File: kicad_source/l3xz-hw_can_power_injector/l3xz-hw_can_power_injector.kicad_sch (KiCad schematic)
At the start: 30 parts, among them CN1 Conn_01x02, CN2 Conn_01x04, CN3 Conn_01x04, CN4 Conn_01x02, CN5 Conn_01x04, CN6 Conn_01x04, U1 RAA211650

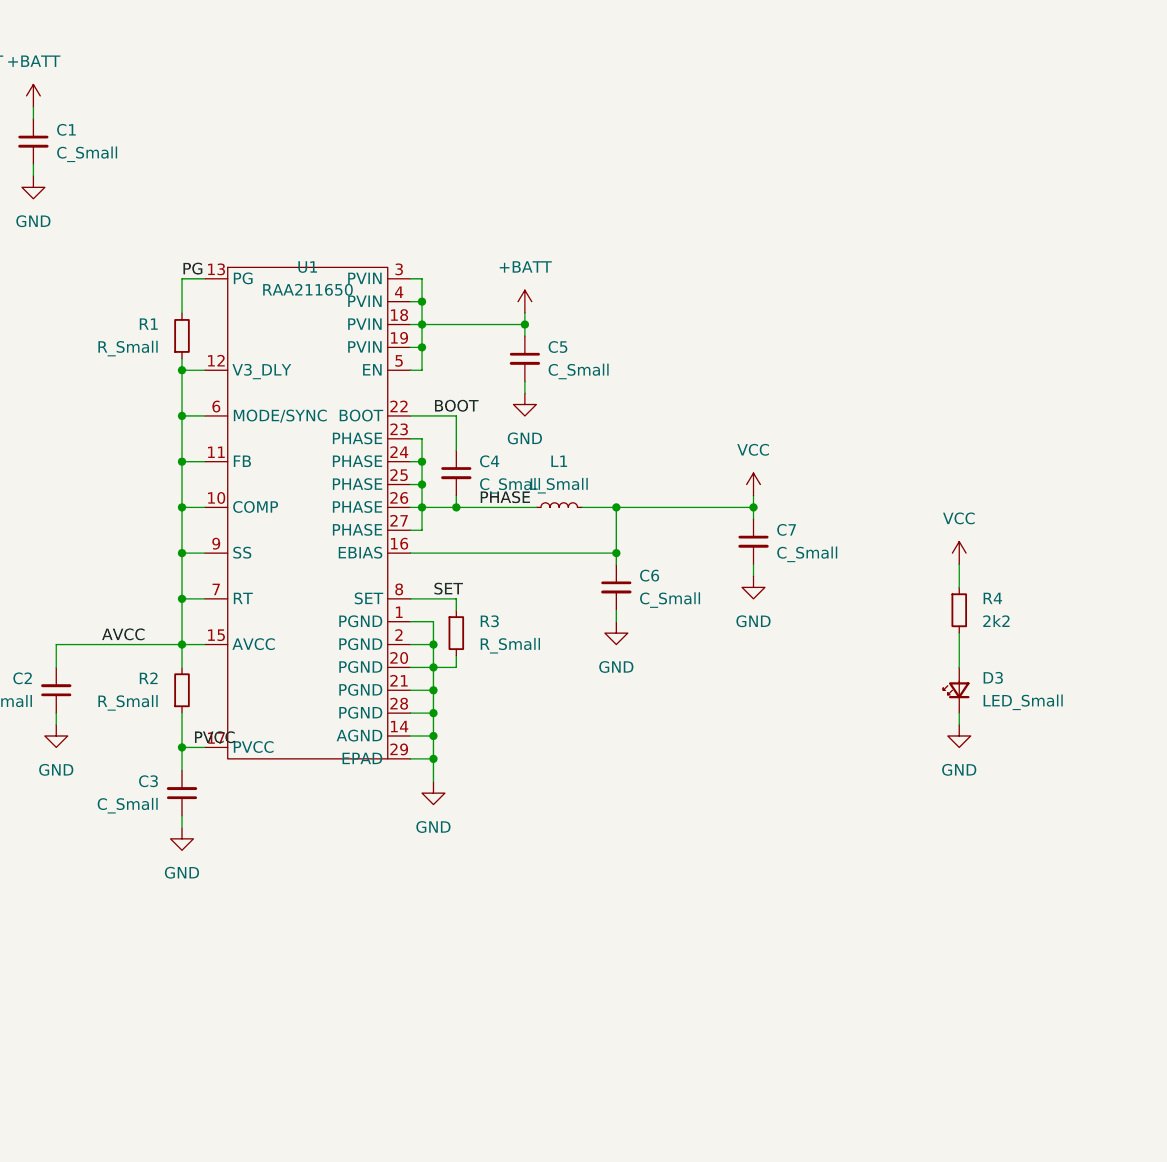
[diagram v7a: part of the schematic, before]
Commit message: added TVS diode and capacitors, updated layout
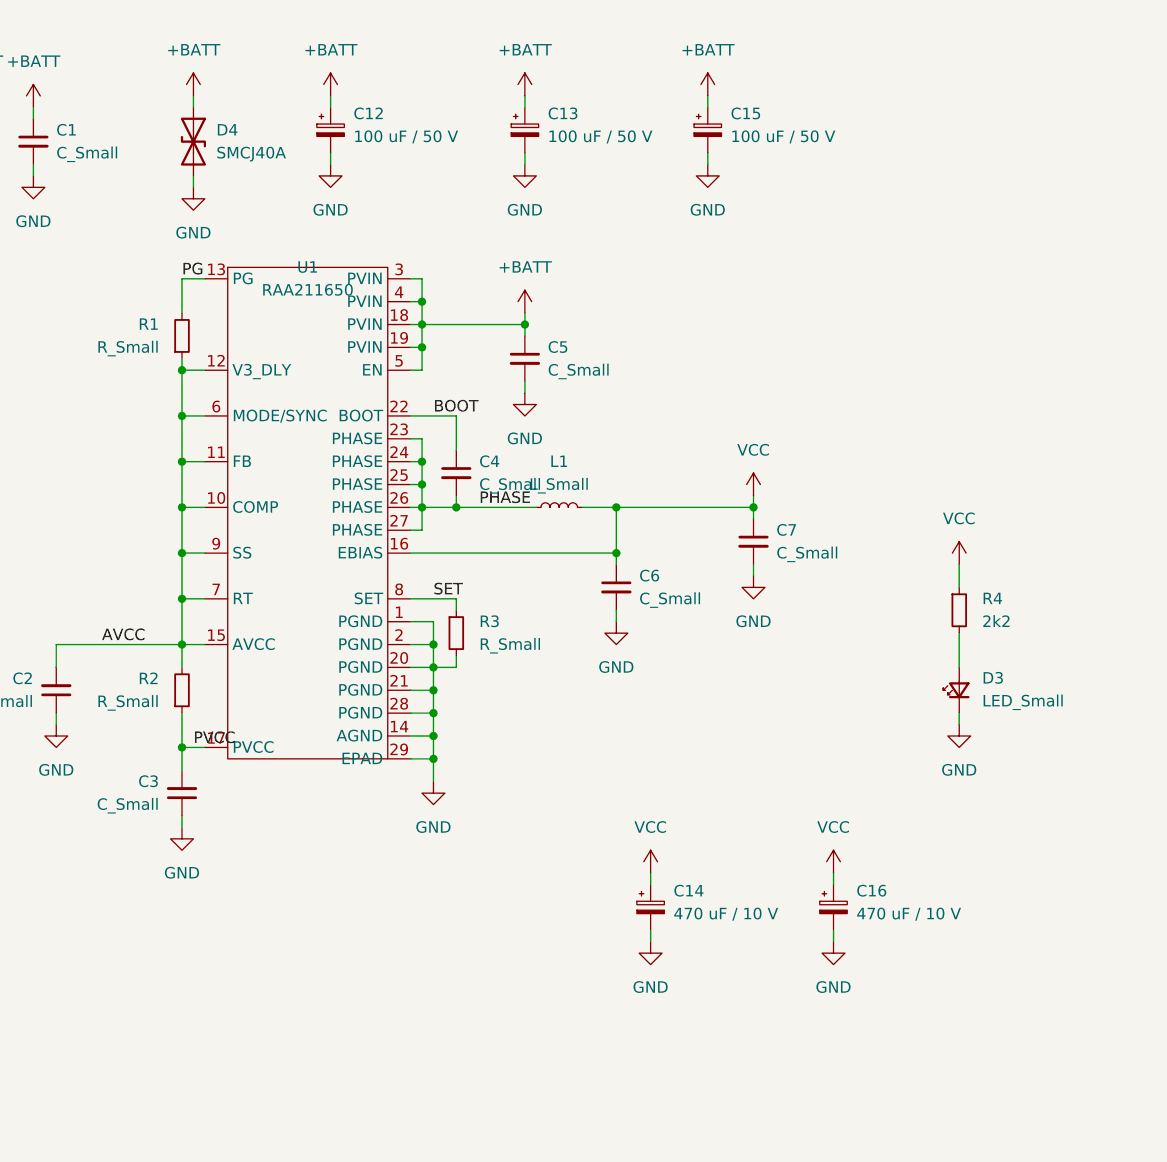
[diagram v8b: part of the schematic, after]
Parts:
- added C12, C13, C15: 100 uF / 50 V, Capacitor_SMD:CP_Elec_10x10, symbol Device:C_Polarized_Small
- added C14, C16: 470 uF / 10 V, Capacitor_SMD:CP_Elec_8x10, symbol Device:C_Polarized_Small
- added D4: SMCJ40A, Diode_SMD:D_SMC, symbol Device:D_TVS
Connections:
- net +BATT: now also C12.1, C13.1, C15.1, D4.1 (A1)
- net GND: now also C12.2, C13.2, C14.2, C15.2, C16.2, D4.2 (A2)
- net VCC: now also C14.1, C16.1
